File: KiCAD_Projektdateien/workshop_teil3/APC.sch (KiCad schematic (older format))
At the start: 20 parts, among them J1 Conn_01x02, SW1 SW_SPDT, U1 NE556

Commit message: Created fabrication files
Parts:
- added FID1, FID2, FID3: Fiducial, Fiducial:Fiducial_1mm_Mask2mm, symbol Mechanical:Fiducial
- BT1: Distributor (none) -> Mouser; Manufacturer (none) -> Eagle Plastic Devices; NP (none) -> No; Order Nr. (none) -> 12BH611-GR; Part Nr. (none) -> 12BH611-GR
- C1: Distributor (none) -> Mouser; Manufacturer (none) -> Wurth Elektronik; NP (none) -> No; Order Nr. (none) -> 710-885012206040; Part Nr. (none) -> 885012206040
- C2: Distributor (none) -> Mouser; Manufacturer (none) -> Wurth Elektronik; NP (none) -> No; Order Nr. (none) -> 710-885012206046; Part Nr. (none) -> 885012206046
- C3: Distributor (none) -> Mouser; Manufacturer (none) -> Wurth Elektronik; NP (none) -> No; Order Nr. (none) -> 710-865080340001; Part Nr. (none) -> 865080340001
- H1, H2, H3, H4, J1, TP1, TP2, TP3, TP4, TP5: NP (none) -> Yes
- R1: Distributor (none) -> Mouser; Manufacturer (none) -> Panasonic; NP (none) -> No; Order Nr. (none) -> 667-ERJ-U02D7500X; Part Nr. (none) -> ERJ-U02D7500X
- RV1, RV2: Distributor (none) -> Mouser; Manufacturer (none) -> Bourns; NP (none) -> No; Order Nr. (none) -> 652-PTV09A4020UB504; Part Nr. (none) -> PTV09A-4020U-B504
- RV3: Distributor (none) -> Mouser; Manufacturer (none) -> Bourns; NP (none) -> No; Order Nr. (none) -> 652-PTV09A-4020FA502; Part Nr. (none) -> PTV09A-4020F-A502
- SW1: Distributor (none) -> Mouser; Manufacturer (none) -> C&K; NP (none) -> No; Order Nr. (none) -> 611-JS102011SAQN; Part Nr. (none) -> JS102011SAQN
- U1: Distributor (none) -> Mouser; Manufacturer (none) -> TI; NP (none) -> No; Order Nr. (none) -> 595-NE556DR; Part Nr. (none) -> NE556DR
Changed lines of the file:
@@
 F 2 "Package_SO:SOIC-14_3.9x8.7mm_P1.27mm" H 7250 3250 50  0001 C CNN
 F 3 "http://www.ti.com/lit/ds/symlink/ne556.pdf" H 7250 3250 50  0001 C CNN
+F 4 "Mouser" H 7250 3250 50  0001 C CNN "Distributor"
+F 5 "TI" H 7250 3250 50  0001 C CNN "Manufacturer"
+F 6 "No" H 7250 3250 50  0001 C CNN "NP"
+F 7 "595-NE556DR" H 7250 3250 50  0001 C CNN "Order Nr."
+F 8 "NE556DR" H 7250 3250 50  0001 C CNN "Part Nr."
 	2    7250 3250
 	1    0    0    -1
@@
 F 2 "Capacitor_SMD:C_0603_1608Metric_Pad1.05x0.95mm_HandSolder" H 5388 3750 50  0001 C CNN
 F 3 "~" H 5350 3900 50  0001 C CNN
+F 4 "Mouser" H 5350 3900 50  0001 C CNN "Distributor"
+F 5 "Wurth Elektronik" H 5350 3900 50  0001 C CNN "Manufacturer"
+F 6 "No" H 5350 3900 50  0001 C CNN "NP"
+F 7 "710-885012206040" H 5350 3900 50  0001 C CNN "Order Nr."
+F 8 "885012206040" H 5350 3900 50  0001 C CNN "Part Nr."
 	1    5350 3900
 	0    -1   -1   0
@@
 F 2 "Capacitor_SMD:C_0603_1608Metric_Pad1.05x0.95mm_HandSolder" H 7538 3750 50  0001 C CNN
 F 3 "~" H 7500 3900 50  0001 C CNN
+F 4 "Mouser" H 7500 3900 50  0001 C CNN "Distributor"
+F 5 "Wurth Elektronik" H 7500 3900 50  0001 C CNN "Manufacturer"
+F 6 "No" H 7500 3900 50  0001 C CNN "NP"
+F 7 "710-885012206046" H 7500 3900 50  0001 C CNN "Order Nr."
+F 8 "885012206046" H 7500 3900 50  0001 C CNN "Part Nr."
 	1    7500 3900
 	0    1    1    0
@@
 F 2 "Capacitor_SMD:CP_Elec_5x3" H 8188 2900 50  0001 C CNN
 F 3 "~" H 8150 3050 50  0001 C CNN
+F 4 "Mouser" H 8150 3050 50  0001 C CNN "Distributor"
+F 5 "Wurth Elektronik" H 8150 3050 50  0001 C CNN "Manufacturer"
+F 6 "No" H 8150 3050 50  0001 C CNN "NP"
+F 7 "710-865080340001" H 8150 3050 50  0001 C CNN "Order Nr."
+F 8 "865080340001" H 8150 3050 50  0001 C CNN "Part Nr."
 	1    8150 3050
 	0    1    1    0
@@
 F 2 "Connector_Wire:SolderWirePad_1x02_P7.62mm_Drill2.5mm" H 8500 2500 50  0001 C CNN
 F 3 "~" H 8500 2500 50  0001 C CNN
+F 4 "Yes" H 8500 2500 50  0001 C CNN "NP"
 	1    8500 2500
 	0    -1   -1   0
@@
 F 2 "Battery:BatteryHolder_Eagle_12BH611-GR" V 3400 3660 50  0001 C CNN
 F 3 "~" V 3400 3660 50  0001 C CNN
+F 4 "Mouser" H 3400 3600 50  0001 C CNN "Distributor"
+F 5 "Eagle Plastic Devices" H 3400 3600 50  0001 C CNN "Manufacturer"
+F 6 "No" H 3400 3600 50  0001 C CNN "NP"
+F 7 "12BH611-GR" H 3400 3600 50  0001 C CNN "Order Nr."
+F 8 "12BH611-GR" H 3400 3600 50  0001 C CNN "Part Nr."
 	1    3400 3600
 	1    0    0    -1
@@
 F 2 "Button_Switch_SMD:SW_SPDT_CK-JS102011SAQN" H 3400 2900 50  0001 C CNN
 F 3 "~" H 3400 2900 50  0001 C CNN
+F 4 "Mouser" H 3400 2900 50  0001 C CNN "Distributor"
+F 5 "C&K" H 3400 2900 50  0001 C CNN "Manufacturer"
+F 6 "No" H 3400 2900 50  0001 C CNN "NP"
+F 7 "611-JS102011SAQN" H 3400 2900 50  0001 C CNN "Order Nr."
+F 8 "JS102011SAQN" H 3400 2900 50  0001 C CNN "Part Nr."
 	1    3400 2900
 	0    -1   -1   0
@@
 F 2 "Package_SO:SOIC-14_3.9x8.7mm_P1.27mm" H 5100 3250 50  0001 C CNN
 F 3 "http://www.ti.com/lit/ds/symlink/ne556.pdf" H 5100 3250 50  0001 C CNN
+F 4 "Mouser" H 5100 3250 50  0001 C CNN "Distributor"
+F 5 "TI" H 5100 3250 50  0001 C CNN "Manufacturer"
+F 6 "No" H 5100 3250 50  0001 C CNN "NP"
+F 7 "595-NE556DR" H 5100 3250 50  0001 C CNN "Order Nr."
+F 8 "NE556DR" H 5100 3250 50  0001 C CNN "Part Nr."
 	1    5100 3250
 	1    0    0    -1
@@
 F 2 "Resistor_SMD:R_0603_1608Metric_Pad1.05x0.95mm_HandSolder" V 6030 3550 50  0001 C CNN
 F 3 "~" H 6100 3550 50  0001 C CNN
+F 4 "Mouser" H 6100 3550 50  0001 C CNN "Distributor"
+F 5 "Panasonic" H 6100 3550 50  0001 C CNN "Manufacturer"
+F 6 "No" H 6100 3550 50  0001 C CNN "NP"
+F 7 "667-ERJ-U02D7500X" H 6100 3550 50  0001 C CNN "Order Nr."
+F 8 "ERJ-U02D7500X" H 6100 3550 50  0001 C CNN "Part Nr."
 	1    6100 3550
 	1    0    0    -1
@@
 F 2 "TestPoint:TestPoint_Pad_D1.5mm" H 3250 2650 50  0001 C CNN
 F 3 "~" H 3250 2650 50  0001 C CNN
+F 4 "Yes" H 3050 2650 50  0001 C CNN "NP"
 	1    3050 2650
 	0    -1   -1   0
@@
 F 2 "TestPoint:TestPoint_Pad_D1.5mm" H 3450 3900 50  0001 C CNN
 F 3 "~" H 3450 3900 50  0001 C CNN
+F 4 "Yes" H 3250 3900 50  0001 C CNN "NP"
 	1    3250 3900
 	0    -1   -1   0
@@
 F 2 "TestPoint:TestPoint_Pad_D1.5mm" H 6350 2500 50  0001 C CNN
 F 3 "~" H 6350 2500 50  0001 C CNN
+F 4 "Yes" H 6150 2500 50  0001 C CNN "NP"
 	1    6150 2500
 	1    0    0    -1
@@
 F 2 "Potentiometer_THT:Potentiometer_Bourns_PTV09A-1_Single_Vertical" H 8400 3500 50  0001 C CNN
 F 3 "~" H 8400 3500 50  0001 C CNN
+F 4 "Mouser" H 8400 3500 50  0001 C CNN "Distributor"
+F 5 "Bourns" H 8400 3500 50  0001 C CNN "Manufacturer"
+F 6 "No" H 8400 3500 50  0001 C CNN "NP"
+F 7 "652-PTV09A4020UB504" H 8400 3500 50  0001 C CNN "Order Nr."
+F 8 "PTV09A-4020U-B504" H 8400 3500 50  0001 C CNN "Part Nr."
 	1    8400 3500
 	-1   0    0    1
@@
 F 2 "Potentiometer_THT:Potentiometer_Bourns_PTV09A-1_Single_Vertical" H 8600 3050 50  0001 C CNN
 F 3 "~" H 8600 3050 50  0001 C CNN
+F 4 "Mouser" H 8600 3050 50  0001 C CNN "Distributor"
+F 5 "Bourns" H 8600 3050 50  0001 C CNN "Manufacturer"
+F 6 "No" H 8600 3050 50  0001 C CNN "NP"
+F 7 "652-PTV09A-4020FA502" H 8600 3050 50  0001 C CNN "Order Nr."
+F 8 "PTV09A-4020F-A502" H 8600 3050 50  0001 C CNN "Part Nr."
 	1    8600 3050
 	-1   0    0    1
@@
 F 2 "TestPoint:TestPoint_Pad_D1.5mm" H 9050 3250 50  0001 C CNN
 F 3 "~" H 9050 3250 50  0001 C CNN
+F 4 "Yes" H 8850 3250 50  0001 C CNN "NP"
 	1    8850 3250
 	0    1    1    0
@@
 F 2 "TestPoint:TestPoint_Pad_D1.5mm" H 6300 3250 50  0001 C CNN
 F 3 "~" H 6300 3250 50  0001 C CNN
+F 4 "Yes" H 6100 3250 50  0001 C CNN "NP"
 	1    6100 3250
 	0    1    1    0
@@
 F 2 "Potentiometer_THT:Potentiometer_Bourns_PTV09A-1_Single_Vertical" H 6100 3000 50  0001 C CNN
 F 3 "~" H 6100 3000 50  0001 C CNN
+F 4 "Mouser" H 6100 3000 50  0001 C CNN "Distributor"
+F 5 "Bourns" H 6100 3000 50  0001 C CNN "Manufacturer"
+F 6 "No" H 6100 3000 50  0001 C CNN "NP"
+F 7 "652-PTV09A4020UB504" H 6100 3000 50  0001 C CNN "Order Nr."
+F 8 "PTV09A-4020U-B504" H 6100 3000 50  0001 C CNN "Part Nr."
 	1    6100 3000
 	1    0    0    -1
@@
 F 2 "MountingHole:MountingHole_3.2mm_M3" H 8400 5950 50  0001 C CNN
 F 3 "~" H 8400 5950 50  0001 C CNN
+F 4 "Yes" H 8400 5950 50  0001 C CNN "NP"
 	1    8400 5950
 	1    0    0    -1
@@
 F 2 "MountingHole:MountingHole_3.2mm_M3" H 9250 5950 50  0001 C CNN
 F 3 "~" H 9250 5950 50  0001 C CNN
+F 4 "Yes" H 9250 5950 50  0001 C CNN "NP"
 	1    9250 5950
 	1    0    0    -1
@@
 F 2 "MountingHole:MountingHole_3.2mm_M3" H 10000 5950 50  0001 C CNN
 F 3 "~" H 10000 5950 50  0001 C CNN
+F 4 "Yes" H 10000 5950 50  0001 C CNN "NP"
 	1    10000 5950
 	1    0    0    -1
@@
 F 2 "MountingHole:MountingHole_3.2mm_M3" H 7650 5950 50  0001 C CNN
 F 3 "~" H 7650 5950 50  0001 C CNN
+F 4 "Yes" H 7650 5950 50  0001 C CNN "NP"
 	1    7650 5950
 	1    0    0    -1
 $EndComp
+$Comp
+L Mechanical:Fiducial FID1
+U 1 1 5D9131F7
+P 8050 5450
+F 0 "FID1" H 8135 5496 50  0000 L CNN
+F 1 "Fiducial" H 8135 5405 50  0000 L CNN
+F 2 "Fiducial:Fiducial_1mm_Mask2mm" H 8050 5450 50  0001 C CNN
+F 3 "~" H 8050 5450 50  0001 C CNN
+F 4 "Yes" H 8050 5450 50  0001 C CNN "NP"
+	1    8050 5450
+	1    0    0    -1
+$EndComp
+$Comp
+L Mechanical:Fiducial FID2
+U 1 1 5D9137E1
+P 8800 5450
+F 0 "FID2" H 8885 5496 50  0000 L CNN
+F 1 "Fiducial" H 8885 5405 50  0000 L CNN
+F 2 "Fiducial:Fiducial_1mm_Mask2mm" H 8800 5450 50  0001 C CNN
+F 3 "~" H 8800 5450 50  0001 C CNN
+F 4 "Yes" H 8800 5450 50  0001 C CNN "NP"
+	1    8800 5450
+	1    0    0    -1
+$EndComp
+$Comp
+L Mechanical:Fiducial FID3
+U 1 1 5D913AE4
+P 9600 5450
+F 0 "FID3" H 9685 5496 50  0000 L CNN
+F 1 "Fiducial" H 9685 5405 50  0000 L CNN
+F 2 "Fiducial:Fiducial_1mm_Mask2mm" H 9600 5450 50  0001 C CNN
+F 3 "~" H 9600 5450 50  0001 C CNN
+F 4 "Yes" H 9600 5450 50  0001 C CNN "NP"
+	1    9600 5450
+	1    0    0    -1
+$EndComp

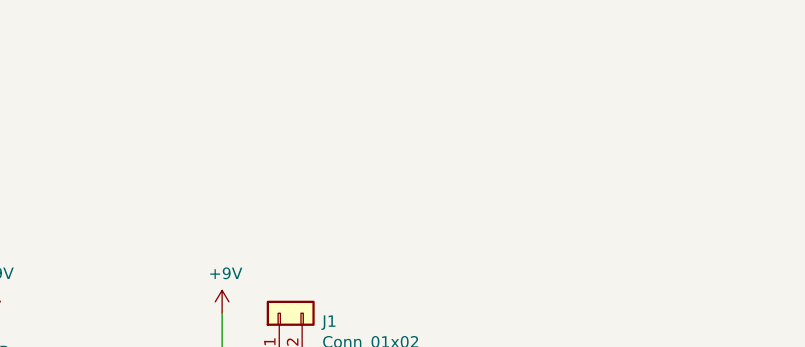
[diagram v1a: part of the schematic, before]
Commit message: Files for workshop3; Fixed typo in teil2 slides
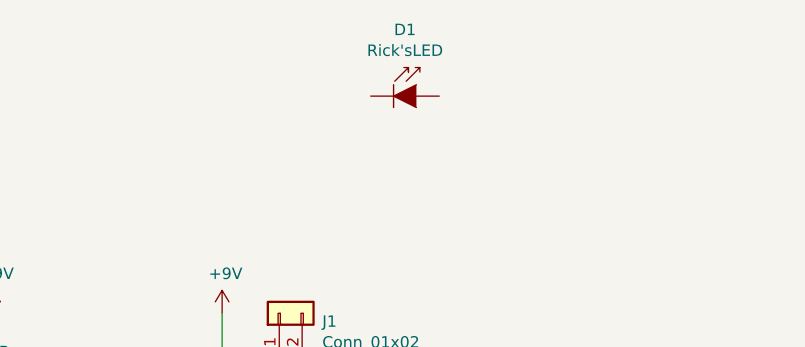
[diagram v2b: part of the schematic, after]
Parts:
- added D1: Rick'sLED, APC:SOIC-12, symbol APC:Rick'sLED
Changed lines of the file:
@@
+	1    0    0    -1
+$EndComp
+$Comp
+L APC:Rick'sLED D1
+U 1 1 5D93CBD1
+P 9100 1550
+F 0 "D1" H 9050 1840 50  0000 C CNN
+F 1 "Rick'sLED" H 9050 1749 50  0000 C CNN
+F 2 "APC:SOIC-12" H 9100 1725 50  0001 C CNN
+F 3 "http://www.osram-os.com/Graphics/XPic5/00181708_0.pdf" H 9050 1550 50  0001 C CNN
+	1    9100 1550
 	1    0    0    -1
 $EndComp
